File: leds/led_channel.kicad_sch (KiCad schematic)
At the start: 10 parts, among them CN5 39302030, CN6 39288020, CN7 39288020, CN8 39288020, U2 BTS70021EPPXUMA1

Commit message: first draft
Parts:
- R24: renamed from R2; value R -> 820; footprint (none) -> Resistor_SMD:R_0603_1608Metric
- renumbered CN5 to CN2, CN6 to CN3, CN7 to CN4, CN8 to CN5, FH5 to FH1, FH6 to FH2, FH7 to FH3, FH8 to FH4, U2 to U8
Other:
- moved on the sheet: CN2, CN3, CN4, CN5

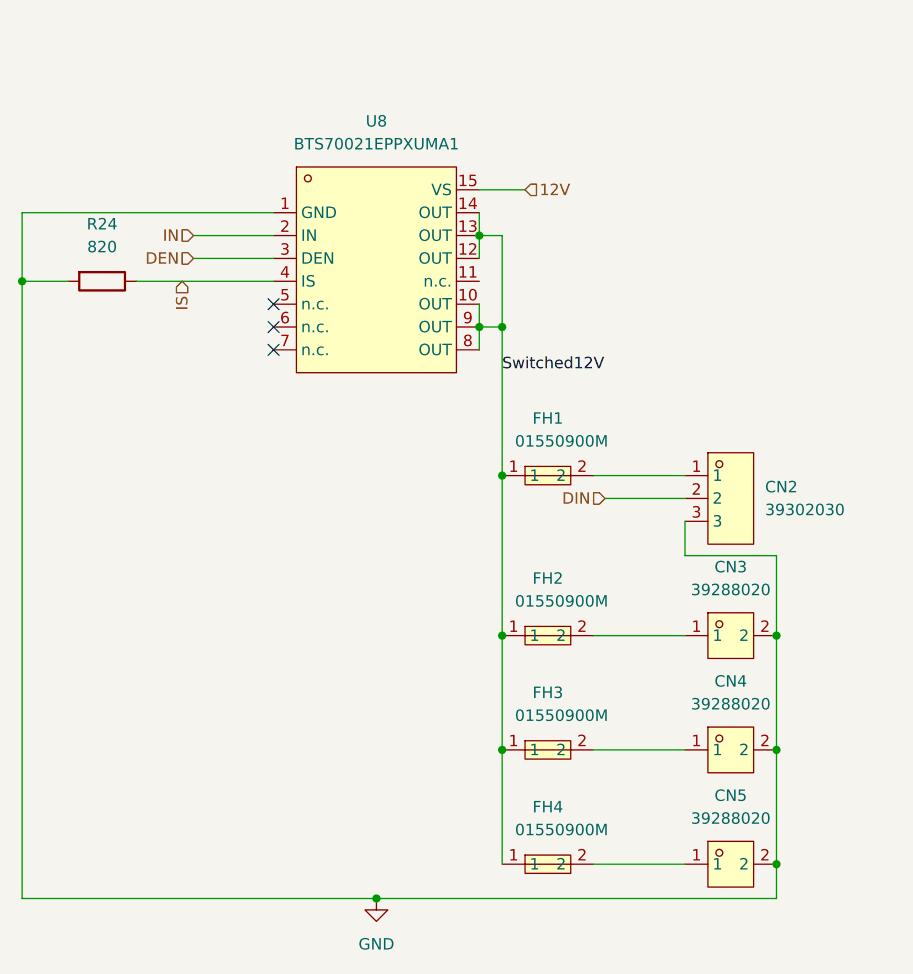
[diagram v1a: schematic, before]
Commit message: Fix errors in LEDs. Revision 0.2 ready to fab.
- [x] Connect VCC on level shifter
- [x] Connect DEN with pull-up
- [x] Add channel on indicator LED - 3.3k
- [x] Flip 3 pin connector
- [x] 82 ohm damping resistor on LED drivers
- [x] Add status LED - white 220 - sinking to ESP
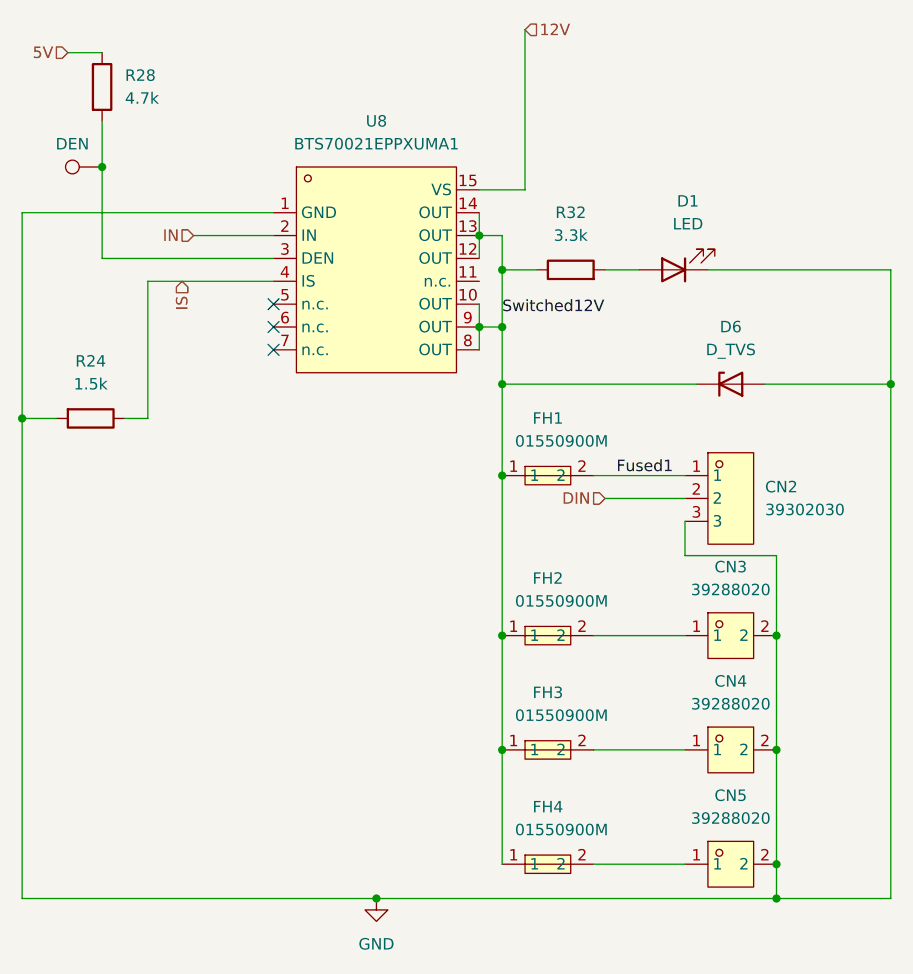
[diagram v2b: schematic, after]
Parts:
- added D1: LED, LED_SMD:LED_0603_1608Metric, symbol Device:LED
- added D6: D_TVS, Diode_SMD:D_SMB, symbol Device:D_Zener
- added R28: 4.7k, Resistor_SMD:R_0603_1608Metric, symbol Device:R
- added R32: 3.3k, Resistor_SMD:R_0603_1608Metric, symbol Device:R
- added TP17: LabeledTestPoint, easyeda2kicad:LabeledTestPoint, symbol easyeda2kicad:LabeledTestPoint
- R24: value 820 -> 1.5k
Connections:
- net GND: now also D1.1 (K), D6.2 (A)
- net Switched12V: now also D6.1 (K), R32.1
- net Fused1: now reaches CN2.1, FH1.2
- net DEN: no longer names the net of U8.3 (DEN)
- net DEN: now also R28.2, TP17.1
- new net: D1.2 (A), R32.2
- new net 5V: R28.1
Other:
- moved on the sheet: R24
